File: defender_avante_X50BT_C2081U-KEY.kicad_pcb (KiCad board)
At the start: 2 copper layers, 172.7 x 61 mm, 80 parts, among them CN301 CONNECTOR_M_006_20_SPECIAL, J300 JUMPER, J301 JUMPER, J302 JUMPER, J303 JUMPER, J304 JUMPER, J305 JUMPER, J306 JUMPER, J307 JUMPER, J308 JUMPER, J309 JUMPER, J310 JUMPER, J311 JUMPER, J312 JUMPER, J313 JUMPER, J314 JUMPER, J315 JUMPER, J316 JUMPER, J317 JUMPER, J318 JUMPER, J319 JUMPER, J320 JUMPER, J321 JUMPER, J322 JUMPER, J323 JUMPER, J324 JUMPER, J325 JUMPER, J326 JUMPER, J327 JUMPER, J328 JUMPER, J329 JUMPER, J330 JUMPER, J331 JUMPER, J332 JUMPER, J333 JUMPER, J334 JUMPER, J335 JUMPER, J336 JUMPER, J337 JUMPER, J338 JUMPER, Q300 BJT_NPN_GENERAL, U300 TM1668

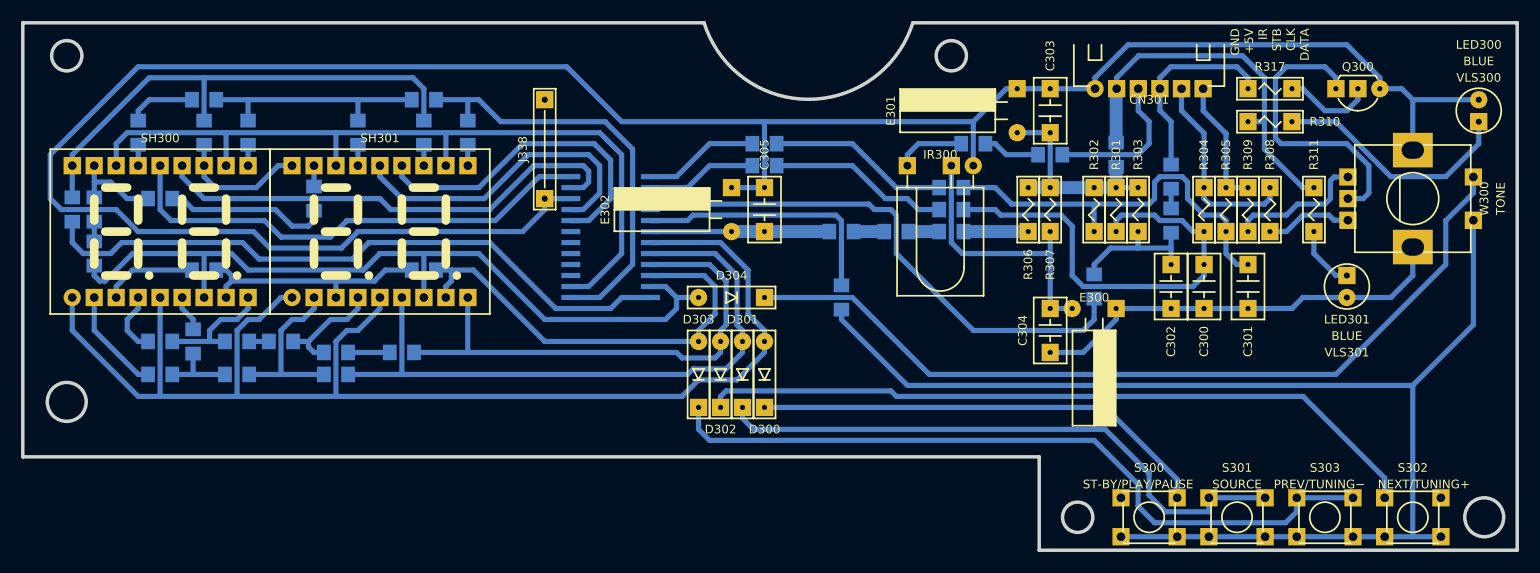
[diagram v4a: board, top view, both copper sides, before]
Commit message: Создан земляной полигон
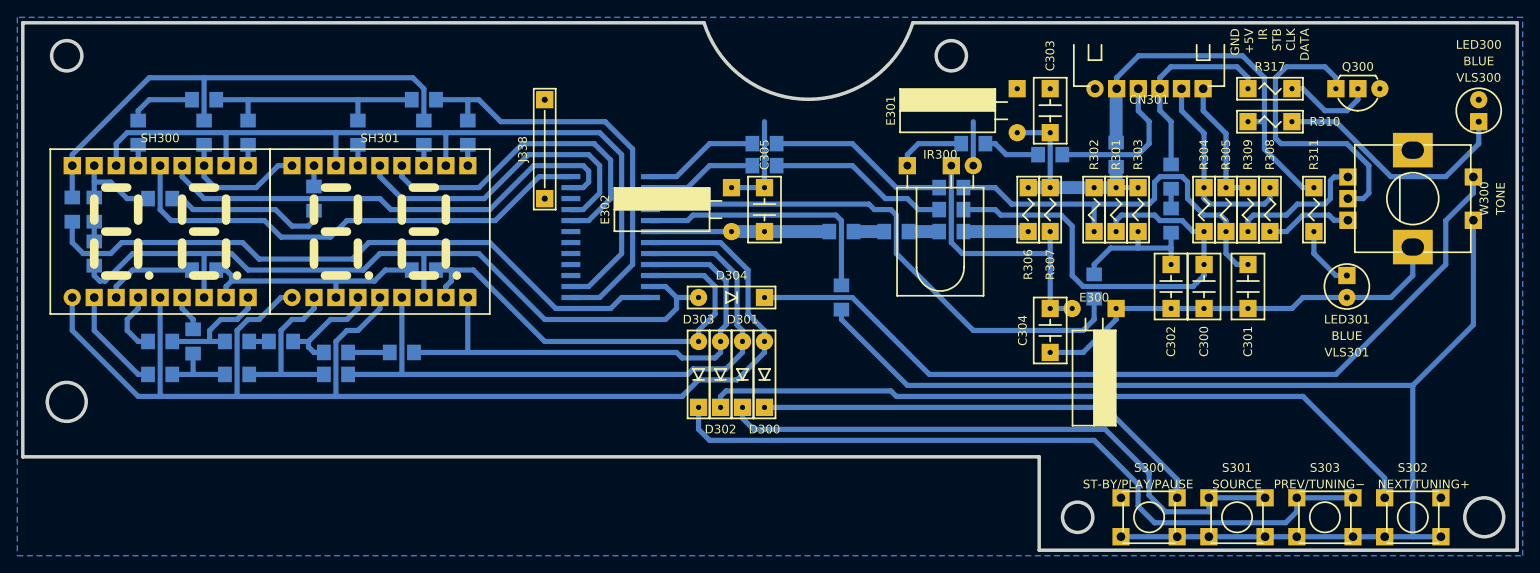
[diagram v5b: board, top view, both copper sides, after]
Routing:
- net COM: track 322.4 -> 66.1 mm
- added copper zone on B.Cu, net COM
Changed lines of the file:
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@@
     (thickness 1.5)
     (drawings 21)
-    (tracks 487)
+    (tracks 458)
     (zones 0)
     (modules 80)
@@
   (segment (start 187.96 88.77) (end 187.96 82.55) (width 1.5) (layer B.Cu) (net 33))
   (segment (start 187.96 91.57) (end 187.96 93.98) (width 1.5) (layer B.Cu) (net 33))
-  (segment (start 171.45 86.36) (end 175.26 82.55) (width 0.6) (layer B.Cu) (net 34))
-  (segment (start 175.26 82.55) (end 176.53 82.55) (width 0.6) (layer B.Cu) (net 34))
-  (segment (start 180.34 82.55) (end 185.52 82.55) (width 0.6) (layer B.Cu) (net 34))
-  (segment (start 143.51 93.98) (end 147.32 93.98) (width 0.6) (layer B.Cu) (net 34))
-  (segment (start 176.53 82.55) (end 180.34 82.55) (width 0.6) (layer B.Cu) (net 34))
-  (segment (start 147.32 93.98) (end 147.32 86.36) (width 0.6) (layer B.Cu) (net 34))
-  (segment (start 171.45 91.44) (end 171.45 86.36) (width 0.6) (layer B.Cu) (net 34))
   (segment (start 180.34 113.03) (end 184.15 113.03) (width 0.6) (layer B.Cu) (net 34))
   (segment (start 184.15 113.03) (end 187.96 109.22) (width 0.6) (layer B.Cu) (net 34))
@@
   (segment (start 194.31 107.95) (end 198.12 107.95) (width 0.6) (layer B.Cu) (net 34))
   (segment (start 198.12 107.95) (end 203.2 107.95) (width 0.6) (layer B.Cu) (net 34))
-  (segment (start 218.44 81.28) (end 214.63 77.47) (width 0.6) (layer B.Cu) (net 34))
-  (segment (start 218.44 82.55) (end 218.44 81.28) (width 0.6) (layer B.Cu) (net 34))
-  (segment (start 185.52 81.28) (end 185.52 82.55) (width 0.6) (layer B.Cu) (net 34))
-  (segment (start 214.63 77.47) (end 189.33 77.47) (width 0.6) (layer B.Cu) (net 34))
-  (segment (start 189.33 77.47) (end 185.52 81.28) (width 0.6) (layer B.Cu) (net 34))
   (segment (start 209.55 106.68) (end 214.63 106.68) (width 0.6) (layer B.Cu) (net 34))
   (segment (start 203.2 107.95) (end 208.28 107.95) (width 0.6) (layer B.Cu) (net 34))
@@
   (segment (start 214.63 106.68) (end 219.71 106.68) (width 0.6) (layer B.Cu) (net 34))
   (segment (start 219.71 106.68) (end 222.25 104.14) (width 0.6) (layer B.Cu) (net 34))
-  (segment (start 222.25 83.82) (end 222.25 89.65) (width 0.6) (layer B.Cu) (net 34))
-  (segment (start 220.98 82.55) (end 222.25 83.82) (width 0.6) (layer B.Cu) (net 34))
-  (segment (start 218.44 82.55) (end 220.98 82.55) (width 0.6) (layer B.Cu) (net 34))
-  (segment (start 222.25 83.82) (end 229.87 83.82) (width 0.6) (layer B.Cu) (net 34))
-  (segment (start 98.425 100.965) (end 100.33 99.06) (width 0.6) (layer B.Cu) (net 34))
-  (segment (start 64.77 90.17) (end 64.77 95.25) (width 0.6) (layer B.Cu) (net 34))
-  (segment (start 119.38 99.06) (end 121.92 96.52) (width 0.6) (layer B.Cu) (net 34))
-  (segment (start 124.46 80.01) (end 74.93 80.01) (width 0.6) (layer B.Cu) (net 34))
-  (segment (start 171.45 86.36) (end 130.81 86.36) (width 0.6) (layer B.Cu) (net 34))
-  (segment (start 100.33 99.06) (end 119.38 99.06) (width 0.6) (layer B.Cu) (net 34))
-  (segment (start 74.93 80.01) (end 64.77 90.17) (width 0.6) (layer B.Cu) (net 34))
-  (segment (start 66.04 96.52) (end 72.39 96.52) (width 0.6) (layer B.Cu) (net 34))
-  (segment (start 130.81 86.36) (end 124.46 80.01) (width 0.6) (layer B.Cu) (net 34))
-  (segment (start 72.39 96.52) (end 74.93 99.06) (width 0.6) (layer B.Cu) (net 34))
-  (segment (start 64.77 95.25) (end 66.04 96.52) (width 0.6) (layer B.Cu) (net 34))
-  (segment (start 74.93 99.06) (end 88.265 99.06) (width 0.6) (layer B.Cu) (net 34))
-  (segment (start 88.265 99.06) (end 90.17 100.965) (width 0.6) (layer B.Cu) (net 34))
-  (segment (start 90.17 100.965) (end 98.425 100.965) (width 0.6) (layer B.Cu) (net 34))
-  (segment (start 121.92 95.25) (end 124.94 95.25) (width 0.6) (layer B.Cu) (net 34))
-  (segment (start 121.92 95.25) (end 121.92 96.52) (width 0.6) (layer B.Cu) (net 34))
+  (segment (start 147.32 93.98) (end 147.32 86.36) (width 0.6) (layer B.Cu) (net 34))
+  (segment (start 143.51 93.98) (end 147.32 93.98) (width 0.6) (layer B.Cu) (net 34))
+  (segment (start 171.45 91.44) (end 171.45 86.36) (width 0.6) (layer B.Cu) (net 34))
+  (zone (net 34) (net_name COM) (layer B.Cu) (hatch edge 0.508)
+    (connect_pads (clearance 0.6))
+    (min_thickness 0.5)
+    (fill yes (arc_segments 32) (thermal_gap 0.6) (thermal_bridge_width 0.6))
+    (polygon
+      (pts
+        (xy 60.96 136.525) (xy 234.95 136.525) (xy 234.95 74.295) (xy 60.96 74.295)
+      )
+    )
+  )
 )
